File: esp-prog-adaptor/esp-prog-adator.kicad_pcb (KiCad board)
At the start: 2 copper layers, 40.6 x 55.9 mm, 6 parts, among them J1 Conn_02x19_Odd_Even, J2 Conn_02x19_Odd_Even, J5 Conn_01x03_Male, J6 Conn_01x03_Male

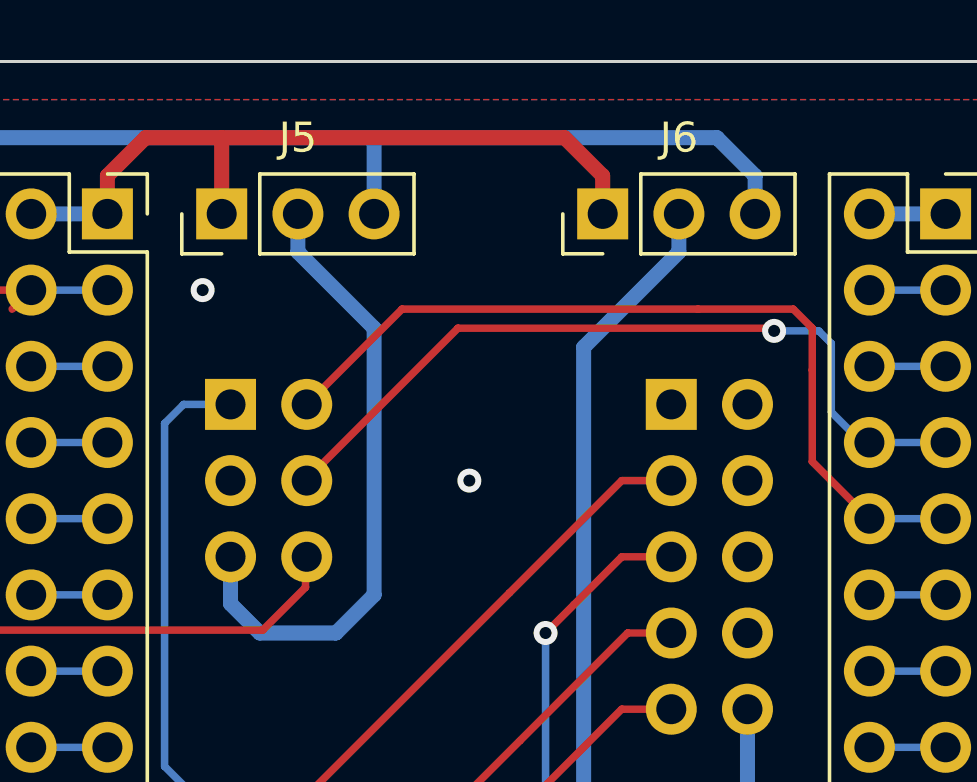
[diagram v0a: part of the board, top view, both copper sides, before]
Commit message: ESP Prog Adaptor 전원 설정 핀 방향 변경
Signed-off-by: Ju, Gyeong-min <jcmh74@gmail.com>
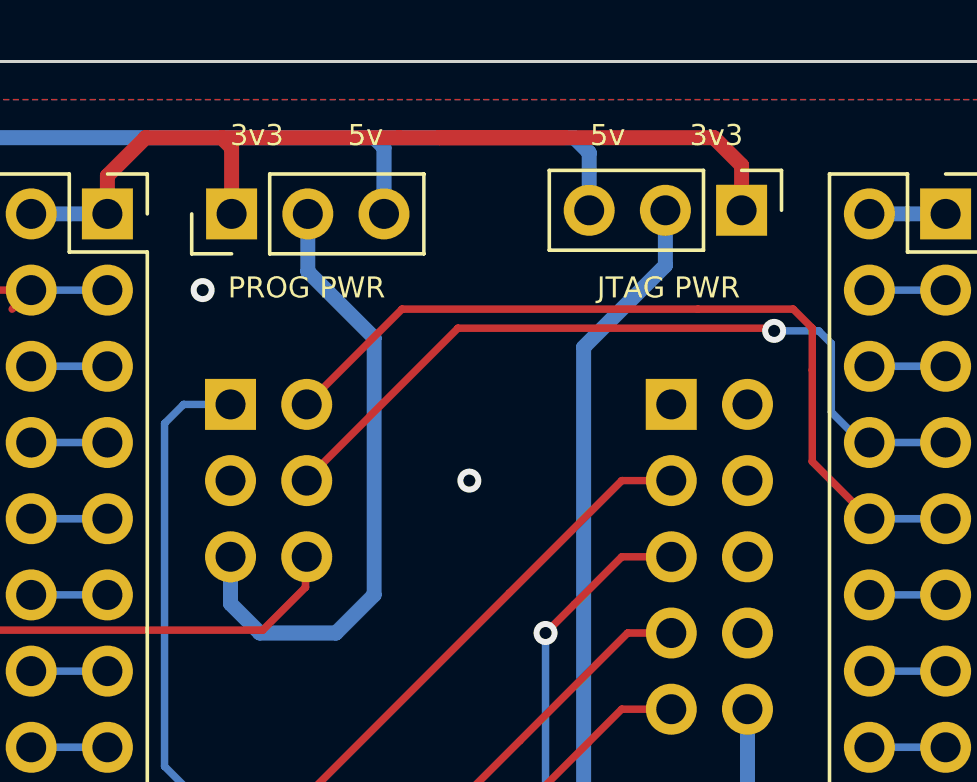
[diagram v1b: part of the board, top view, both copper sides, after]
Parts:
- moved J6 4.63 mm to (107.5, 71.0), turned to 270 degrees
- moved J5 0.33 mm to (90.5, 71.1)
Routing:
- net +3V3: track 36.6 -> 45.6 mm
- net +5V: track 83.2 -> 78.2 mm
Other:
- board text added: "3v3 5v"
- board text added: "5v 3v3"
- board text added: "JTAG PWR"
- board text added: "PROG PWR"
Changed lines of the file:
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@@
   (general
     (thickness 1.6)
-    (drawings 21)
-    (tracks 131)
+    (drawings 25)
+    (tracks 137)
     (zones 0)
     (modules 6)
@@
   )
   (module Connector_PinHeader_2.54mm:PinHeader_1x03_P2.54mm_Vertical (layer F.Cu)
-    (at 90.17 71.12 90)
+    (at 90.5 71.12 90)
     (descr "Through hole straight pin header, 1x03, 2.54mm pitch, single row")
     (tags "Through hole pin header THT 1x03 2.54mm single row")
-    (fp_text reference J5 (at 2.54 2.54 180) (layer F.SilkS)
+    (fp_text reference J5 (at -2.38 2 180) (layer F.SilkS) hide
       (effects (font (size 1 1) (thickness 0.15)))
     )
@@
   )
   (module Connector_PinHeader_2.54mm:PinHeader_1x03_P2.54mm_Vertical (layer F.Cu)
-    (at 102.87 71.12 90)
+    (at 107.5 71 270)
     (descr "Through hole straight pin header, 1x03, 2.54mm pitch, single row")
     (tags "Through hole pin header THT 1x03 2.54mm single row")
-    (fp_text reference J6 (at 2.54 2.54 180) (layer F.SilkS)
+    (fp_text reference J6 (at 2.5 2.54 180) (layer F.SilkS) hide
       (effects (font (size 1 1) (thickness 0.15)))
     )
@@
       (effects (font (size 1 1) (thickness 0.15)))
     )
-    (pad 3 thru_hole oval (at 0 5.08 90) (size 1.7 1.7) (drill 1) (layers *.Cu *.Mask)
+    (pad 3 thru_hole oval (at 0 5.08 270) (size 1.7 1.7) (drill 1) (layers *.Cu *.Mask)
       (net 3 +5V))
-    (pad 2 thru_hole oval (at 0 2.54 90) (size 1.7 1.7) (drill 1) (layers *.Cu *.Mask)
+    (pad 2 thru_hole oval (at 0 2.54 270) (size 1.7 1.7) (drill 1) (layers *.Cu *.Mask)
       (net 39 /Vjtag))
-    (pad 1 thru_hole rect (at 0 0 90) (size 1.7 1.7) (drill 1) (layers *.Cu *.Mask)
+    (pad 1 thru_hole rect (at 0 0 270) (size 1.7 1.7) (drill 1) (layers *.Cu *.Mask)
       (net 2 +3V3))
     (model ${KISYS3DMOD}/Connector_PinHeader_2.54mm.3dshapes/PinHeader_1x03_P2.54mm_Vertical.wrl
@@
     )
   )
+  (gr_text "3v3       5v" (at 93 68.5) (layer F.SilkS)
+    (effects (font (size 0.7 0.7) (thickness 0.1)))
+  )
+  (gr_text "JTAG PWR" (at 105.065 73.58) (layer F.SilkS)
+    (effects (font (size 0.7 0.7) (thickness 0.1)))
+  )
+  (gr_text "PROG PWR" (at 93 73.58) (layer F.SilkS)
+    (effects (font (size 0.7 0.7) (thickness 0.1)))
+  )
+  (gr_text "5v       3v3" (at 105 68.5) (layer F.SilkS)
+    (effects (font (size 0.7 0.7) (thickness 0.1)))
+  )
   (gr_text G15 (at 115.57 109.22) (layer F.SilkS)
     (effects (font (size 1 1) (thickness 0.15)) (justify left))
@@
   (via (at 89.535 73.66) (size 0.8) (drill 0.4) (layers F.Cu B.Cu) (net 1))
   (via (at 98.425 80.01) (size 0.8) (drill 0.4) (layers F.Cu B.Cu) (net 1))
-  (segment (start 91.44 68.58) (end 101.6 68.58) (width 0.5) (layer F.Cu) (net 2))
-  (segment (start 102.87 69.85) (end 102.87 71.12) (width 0.5) (layer F.Cu) (net 2) (status 20))
-  (segment (start 101.6 68.58) (end 102.87 69.85) (width 0.5) (layer F.Cu) (net 2))
-  (segment (start 90.17 68.58) (end 101.6 68.58) (width 0.25) (layer F.Cu) (net 2))
-  (segment (start 90.17 71.12) (end 90.17 68.58) (width 0.5) (layer F.Cu) (net 2) (status 10))
   (segment (start 86.36 71.12) (end 86.36 69.85) (width 0.5) (layer F.Cu) (net 2) (status 10))
   (segment (start 86.36 69.85) (end 87.63 68.58) (width 0.5) (layer F.Cu) (net 2))
   (segment (start 87.63 68.58) (end 91.44 68.58) (width 0.5) (layer F.Cu) (net 2))
   (segment (start 83.82 71.12) (end 86.36 71.12) (width 0.5) (layer B.Cu) (net 2) (status 30))
-  (segment (start 106.68 68.58) (end 96.52 68.58) (width 0.5) (layer B.Cu) (net 3))
-  (segment (start 107.95 71.12) (end 107.95 69.85) (width 0.5) (layer B.Cu) (net 3) (status 10))
-  (segment (start 107.95 69.85) (end 106.68 68.58) (width 0.5) (layer B.Cu) (net 3))
+  (segment (start 100.08 68.58) (end 101.6 68.58) (width 0.25) (layer F.Cu) (net 2))
+  (segment (start 90.17 68.58) (end 100.08 68.58) (width 0.25) (layer F.Cu) (net 2))
+  (segment (start 90.5 68.91) (end 90.17 68.58) (width 0.5) (layer F.Cu) (net 2))
+  (segment (start 90.5 71.12) (end 90.5 68.91) (width 0.5) (layer F.Cu) (net 2))
+  (segment (start 91.44 68.58) (end 96.08 68.58) (width 0.5) (layer F.Cu) (net 2))
+  (segment (start 97.42 68.58) (end 106.58 68.58) (width 0.5) (layer F.Cu) (net 2))
+  (segment (start 106.58 68.58) (end 107.5 69.5) (width 0.5) (layer F.Cu) (net 2))
+  (segment (start 107.5 69.5) (end 107.5 71) (width 0.5) (layer F.Cu) (net 2))
+  (segment (start 96.08 68.58) (end 97.42 68.58) (width 0.5) (layer F.Cu) (net 2))
+  (segment (start 97.42 68.58) (end 101.6 68.58) (width 0.5) (layer F.Cu) (net 2))
   (segment (start 96.52 68.58) (end 95.25 68.58) (width 0.5) (layer B.Cu) (net 3))
-  (segment (start 81.28 116.205) (end 81.28 69.85) (width 0.5) (layer B.Cu) (net 3) (status 1000000))
-  (segment (start 95.25 68.58) (end 82.55 68.58) (width 0.5) (layer B.Cu) (net 3) (status 1000000))
-  (segment (start 82.55 68.58) (end 81.28 69.85) (width 0.5) (layer B.Cu) (net 3) (status 1000000))
-  (segment (start 81.915 116.84) (end 83.82 116.84) (width 0.5) (layer B.Cu) (net 3) (status 1000020))
-  (segment (start 81.28 116.205) (end 81.915 116.84) (width 0.5) (layer B.Cu) (net 3) (status 1000000))
+  (segment (start 101.92 68.58) (end 96.52 68.58) (width 0.5) (layer B.Cu) (net 3))
+  (segment (start 102.42 71) (end 102.42 69.08) (width 0.5) (layer B.Cu) (net 3))
+  (segment (start 102.42 69.08) (end 101.92 68.58) (width 0.5) (layer B.Cu) (net 3))
+  (segment (start 81.28 116.205) (end 81.28 69.85) (width 0.5) (layer B.Cu) (net 3))
+  (segment (start 81.28 116.205) (end 81.915 116.84) (width 0.5) (layer B.Cu) (net 3))
+  (segment (start 81.915 116.84) (end 83.82 116.84) (width 0.5) (layer B.Cu) (net 3) (status 20))
+  (segment (start 82.55 68.58) (end 81.28 69.85) (width 0.5) (layer B.Cu) (net 3))
+  (segment (start 95.25 68.58) (end 82.55 68.58) (width 0.5) (layer B.Cu) (net 3))
   (segment (start 83.82 116.84) (end 86.36 116.84) (width 0.5) (layer B.Cu) (net 3) (status 30))
-  (segment (start 95.25 71.12) (end 95.25 68.58) (width 0.5) (layer B.Cu) (net 3))
+  (segment (start 95.58 68.91) (end 95.25 68.58) (width 0.5) (layer B.Cu) (net 3))
+  (segment (start 95.58 71.12) (end 95.58 68.91) (width 0.5) (layer B.Cu) (net 3))
   (segment (start 83.82 73.66) (end 86.36 73.66) (width 0.25) (layer B.Cu) (net 4) (status 30))
   (segment (start 86.995 73.66) (end 86.36 73.66) (width 0.25) (layer B.Cu) (net 4) (status 30))
@@
   (segment (start 105.156 82.55) (end 103.505 82.55) (width 0.25) (layer F.Cu) (net 37) (status 10))
   (segment (start 101.9175 84.1375) (end 100.965 85.09) (width 0.25) (layer F.Cu) (net 37))
-  (segment (start 92.71 71.12) (end 92.71 72.39) (width 0.5) (layer B.Cu) (net 38) (status 10))
   (segment (start 93.98 85.09) (end 91.44 85.09) (width 0.5) (layer B.Cu) (net 38))
+  (segment (start 95.25 75.25) (end 95.25 83.82) (width 0.5) (layer B.Cu) (net 38))
+  (segment (start 93.04 71.12) (end 93.04 73.04) (width 0.5) (layer B.Cu) (net 38))
+  (segment (start 93.04 73.04) (end 95.25 75.25) (width 0.5) (layer B.Cu) (net 38))
+  (segment (start 90.464 82.55) (end 90.464 84.114) (width 0.5) (layer B.Cu) (net 38) (status 10))
+  (segment (start 90.464 84.114) (end 91.44 85.09) (width 0.5) (layer B.Cu) (net 38))
   (segment (start 95.25 83.82) (end 93.98 85.09) (width 0.5) (layer B.Cu) (net 38))
-  (segment (start 95.25 74.93) (end 95.25 83.82) (width 0.5) (layer B.Cu) (net 38))
-  (segment (start 92.71 72.39) (end 95.25 74.93) (width 0.5) (layer B.Cu) (net 38))
-  (segment (start 90.464 84.114) (end 91.44 85.09) (width 0.5) (layer B.Cu) (net 38))
-  (segment (start 90.464 82.55) (end 90.464 84.114) (width 0.5) (layer B.Cu) (net 38) (status 10))
-  (segment (start 105.41 71.12) (end 105.41 72.39) (width 0.5) (layer B.Cu) (net 39) (status 10))
-  (segment (start 105.41 72.39) (end 102.235 75.565) (width 0.5) (layer B.Cu) (net 39))
   (segment (start 102.235 75.565) (end 102.235 90.17) (width 0.5) (layer B.Cu) (net 39))
+  (segment (start 104.96 71) (end 104.96 72.84) (width 0.5) (layer B.Cu) (net 39))
+  (segment (start 104.96 72.84) (end 102.235 75.565) (width 0.5) (layer B.Cu) (net 39))
+  (segment (start 103.505 91.44) (end 106.426 91.44) (width 0.5) (layer B.Cu) (net 39))
+  (segment (start 107.696 87.63) (end 107.696 90.17) (width 0.5) (layer B.Cu) (net 39))
+  (segment (start 107.696 90.17) (end 106.426 91.44) (width 0.5) (layer B.Cu) (net 39))
   (segment (start 102.235 90.17) (end 103.505 91.44) (width 0.5) (layer B.Cu) (net 39))
-  (segment (start 107.696 90.17) (end 106.426 91.44) (width 0.5) (layer B.Cu) (net 39))
-  (segment (start 107.696 87.63) (end 107.696 90.17) (width 0.5) (layer B.Cu) (net 39))
-  (segment (start 103.505 91.44) (end 106.426 91.44) (width 0.5) (layer B.Cu) (net 39))
   (segment (start 111.76 76.2) (end 114.3 76.2) (width 0.25) (layer B.Cu) (net 40) (status 30))
   (zone (net 1) (net_name GND) (layer F.Cu) (hatch edge 0.508)

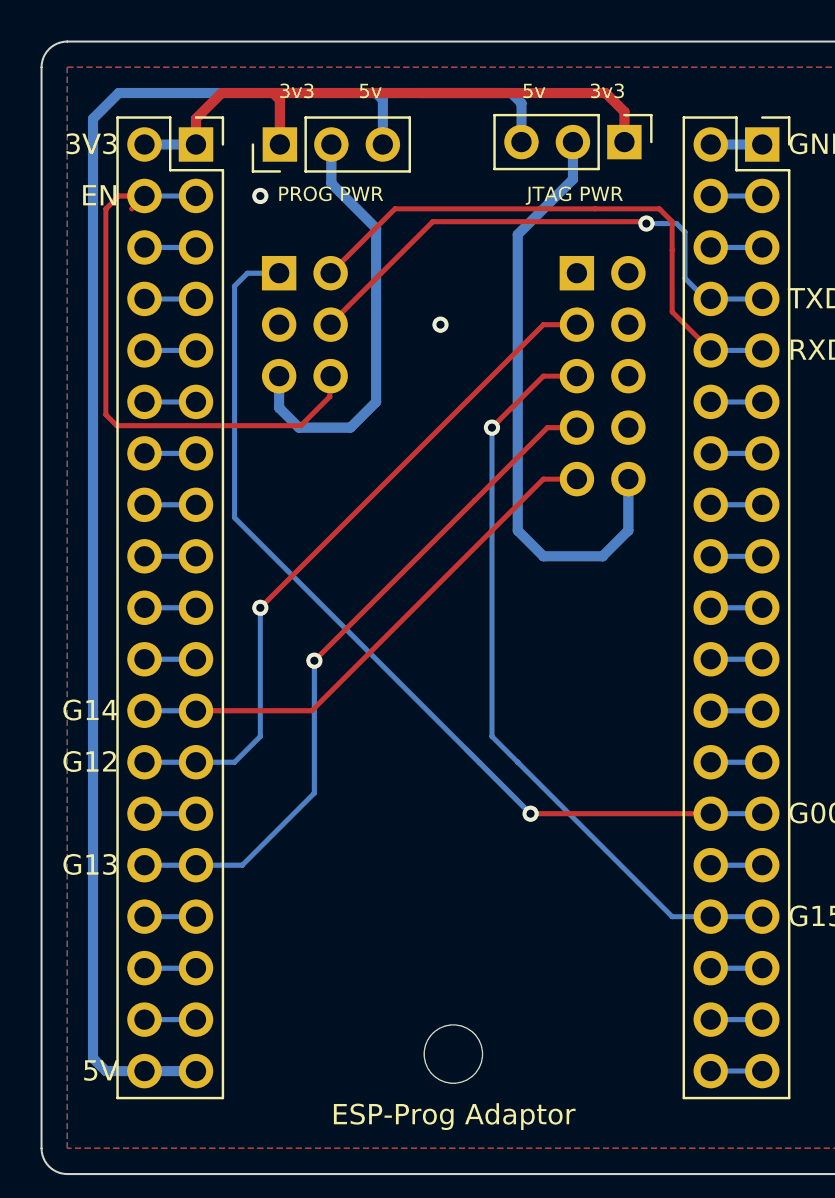
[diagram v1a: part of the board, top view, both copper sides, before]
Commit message: * esp-debug-adapter : 트레이스 개선 * joystick-input : SMD로 변경
Signed-off-by: Ju, Gyeong-min <jcmh74@gmail.com>
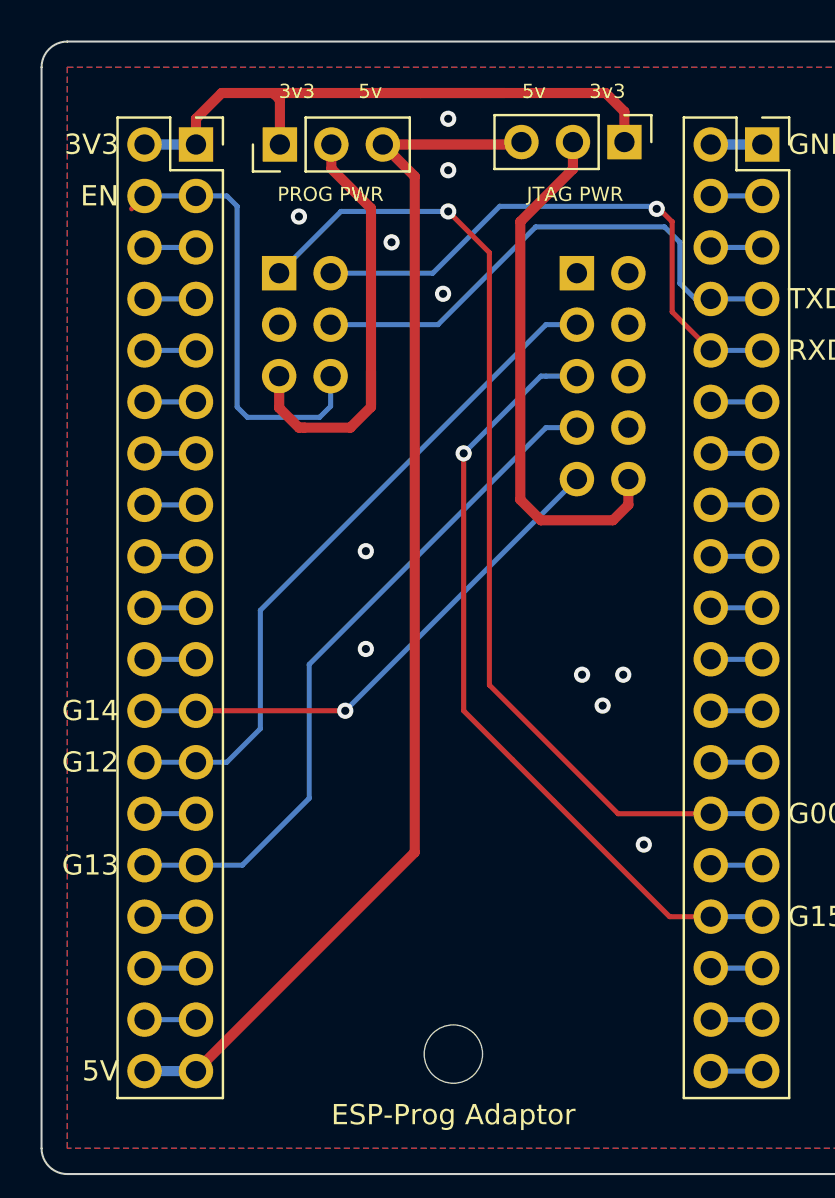
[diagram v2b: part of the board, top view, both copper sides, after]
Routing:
- net +5V: track 78.2 -> 60.3 mm
- net /EN: track 29.3 -> 22.8 mm
- net /Vjtag: track 29.4 -> 26.1 mm
- net /Vprog: track 20.9 -> 22.4 mm
- net /TDO(G15): track 37.5 -> 38.8 mm
- net /TXD: track 26.7 -> 26.0 mm, vias 1 -> 0
- net /G00: track 50.5 -> 49.9 mm
- net /TDI(G12): track 34.0 -> 33.7 mm, vias 1 -> 0
- net /TMS(G14): track 26.1 -> 26.3 mm, vias 0 -> 1
- net /RXD: track 28.1 -> 28.2 mm, vias 0 -> 1
- net /TCK(G13): vias 1 -> 0
- net GND: vias 2 -> 11

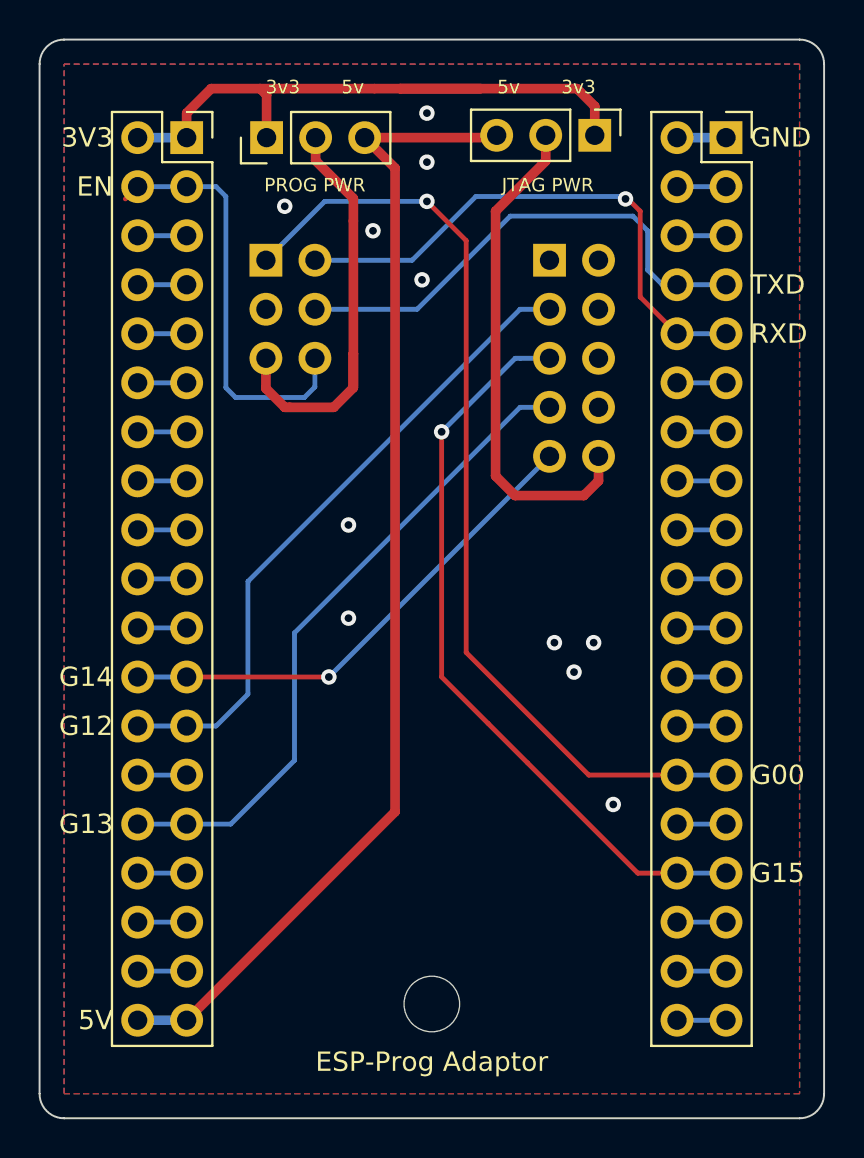
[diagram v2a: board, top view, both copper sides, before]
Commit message: kicad 6로 마이그레이션
Signed-off-by: Ju, Gyeong-min <jcmh74@gmail.com>
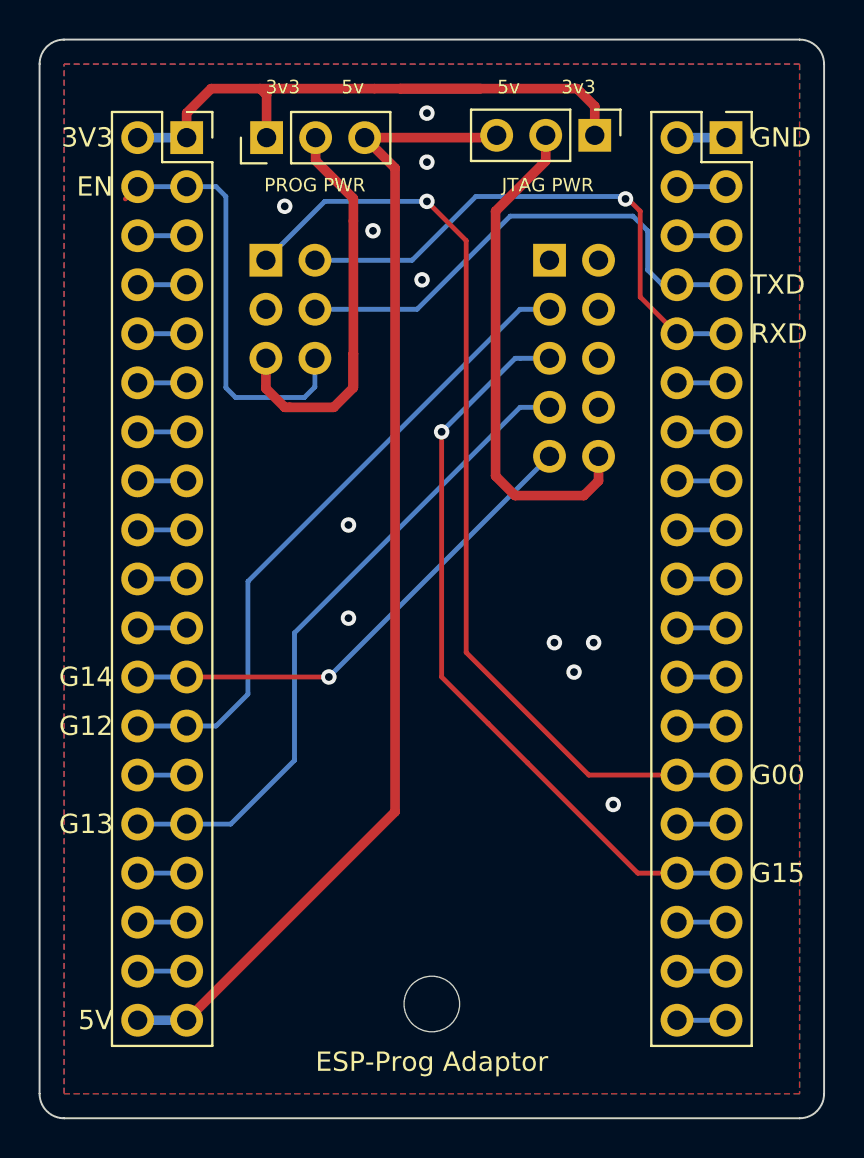
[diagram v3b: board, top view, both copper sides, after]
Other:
- net class Default removed
- net class Power removed

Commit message: 도면 시트 설명 추가
Signed-off-by: Ju, Gyeong-min <jcmh74@gmail.com>
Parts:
- moved J1 59.8 mm to (145.5, 79.7)
- moved J2 59.8 mm to (173.5, 79.7)
- moved J5 59.8 mm to (149.7, 79.7)
- moved J6 59.8 mm to (166.7, 79.5)
- moved JTAG1 59.8 mm to (164.3, 86.0)
- moved PROG1 59.8 mm to (149.6, 86.0)
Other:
- board text added: "ESP-Prog Adaptor Rev.2"
- board text removed: "ESP-Prog Adaptor"
